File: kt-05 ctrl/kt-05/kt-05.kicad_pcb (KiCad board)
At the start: 4 copper layers, 50.3 x 71.2 mm, 76 parts, among them CN10 YTC1P-6030-01, CN11 YTC1P-6030-01, CN12 YTC1P-6030-01, CN13 YTC1P-6030-01, CN14 YTC1P-6030-01, CN15 MIDI IN, CN16 MIDI OUT, CN3 YTC1P-6030-01, CN4 Pogo Pin Receptor Right, CN5 YTC1P-6030-01, CN6 YTC1P-6030-01, CN7 YTC1P-6030-01, CN8 YTC1P-6030-01, CN9 YTC1P-6030-01, J1 Conn_01x06, Q1 AO3401A, Q2 AO3401A, Q3 AO3401A, SW1 ESP RST, SW2 ESP BOOT, U1 SK6812MINI-HS, U10 H3V3U10B, U11 H3V3U10B, U12 H3V3U10B, U13 H3V3U10B, U14 H3V3U10B, U15 H3V3U10B, U16 H3V3U10B, U17 H3V3U10B, U18 H3V3U10B, U19 H3V3U10B, U2 AP2112K-3.3, U20 H3V3U10B, U21 H3V3U10B, U22 H3V3U10B, U23 H3V3U10B, U3 MCP73831-2-OT, U4 PS-5850SVB-6PL, U5 H11L1S(TA), U6 ATtiny1616-M, U7 H3V3U10B, U8 ESP32-S3-MINI-1, U9 Pogo Pin Left

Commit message: ch
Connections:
- CN4 pad 1: SCL1 -> GND
- CN4 pad 2: SDA1 -> VRIGHT
- CN4 pad 3: VRIGHT -> SDA1
- CN4 pad 4: GND -> SCL1
- U9 pad 1: GND -> SCL0
- U9 pad 2: VLEFT -> SDA0
- U9 pad 3: SDA0 -> VLEFT
- U9 pad 4: SCL0 -> GND
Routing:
- net SCL0: track 55.4 -> 66.5 mm
- net SCL1: track 30.7 -> 38.8 mm
- net SDA0: track 62.2 -> 65.0 mm
- net GND: track 141.9 -> 140.0 mm, vias 96 -> 95
- net VLEFT: track 3.34 -> 4.82 mm, vias 0 -> 2
- net VRIGHT: track 3.27 -> 4.75 mm
- net SDA1: track 32.6 -> 33.2 mm, vias 3 -> 4

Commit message: many
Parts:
- added R10: 10K, Resistor_SMD:R_0402_1005Metric, F.Cu at (66.8, 36.6)
- added R11: 10K, Resistor_SMD:R_0402_1005Metric, F.Cu at (66.8, 38.6)
- moved J1 2.54 mm to (90.0, 84.6)
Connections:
- U8 pad 17: unconnected-(U8-IO13-Pad17) -> BAT_DET
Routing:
- net BAT_DET: track 0.00 -> 19.0 mm, vias 0 -> 2
- net VBAT: track 23.2 -> 27.7 mm
- net GND: track 140.0 -> 143.4 mm
- net SDA0: track 65.0 -> 67.5 mm
- net +3.3V: track 54.2 -> 56.7 mm
- net UPDI: track 74.5 -> 77.0 mm
- net SCL0: track 66.5 -> 69.0 mm
- net TXD: track 38.6 -> 40.5 mm
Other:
- outline, holes or cut-outs redrawn
- board text added: "0.1"
- board text added: "2/2026"
- board text added: "3.3V"
- board text added: "BATTERY HERE"
- board text added: "CC-BY-NC-SA 4.0"
- board text added: "CORE"
- board text added: "DESIGN"
- board text added: "ESP BOOT"
- board text added: "ESP RST"
- board text added: "GITHUB.COM/TORBERS"
- board text added: "GND"
- board text added: "IN"
- board text added: "MIDI"
- board text added: "OPEN SOURCE"
- board text added: "OUT"
- board text added: "POWER"
- board text added: "SCL"
- board text added: "SDA"
- board text added: "SHEPHERD MIX MODULE"
- board text added: "SOURCE FILES"
- board text added: "TEST TYPE"
- board text added: "TORBERS"
- board text added: "TXD"
- board text added: "TYPE-C"
- board text added: "UPDI"
- board text added: "USB"
- board text added: "VBUS"

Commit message: prod
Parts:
- moved R7 15.8 mm to (92.1, 57.3), turned to -90 degrees
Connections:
- U6 pad 1: A15 -> SCL0
- U6 pad 10: unconnected-(U6-PB4-Pad10) -> A16
- U6 pad 13: SDA0 -> A15
- U6 pad 14: SCL0 -> A14
- U6 pad 2: A16 -> unconnected-(U6-PA3-Pad2)
- U6 pad 20: A14 -> SDA0
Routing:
- net A15: track 6.33 -> 38.1 mm, vias 0 -> 4
- net A16: track 11.0 -> 21.8 mm, vias 0 -> 2
- net SCL0: track 69.0 -> 78.2 mm, vias 3 -> 5
- net A14: track 28.4 -> 37.5 mm, vias 2 -> 4
- net SDA0: track 67.5 -> 75.2 mm, vias 5 -> 7
- net UPDI: track 77.0 -> 78.0 mm
- net D10: track 8.93 -> 8.43 mm
- net GND: track 143.4 -> 143.5 mm, vias 95 -> 94

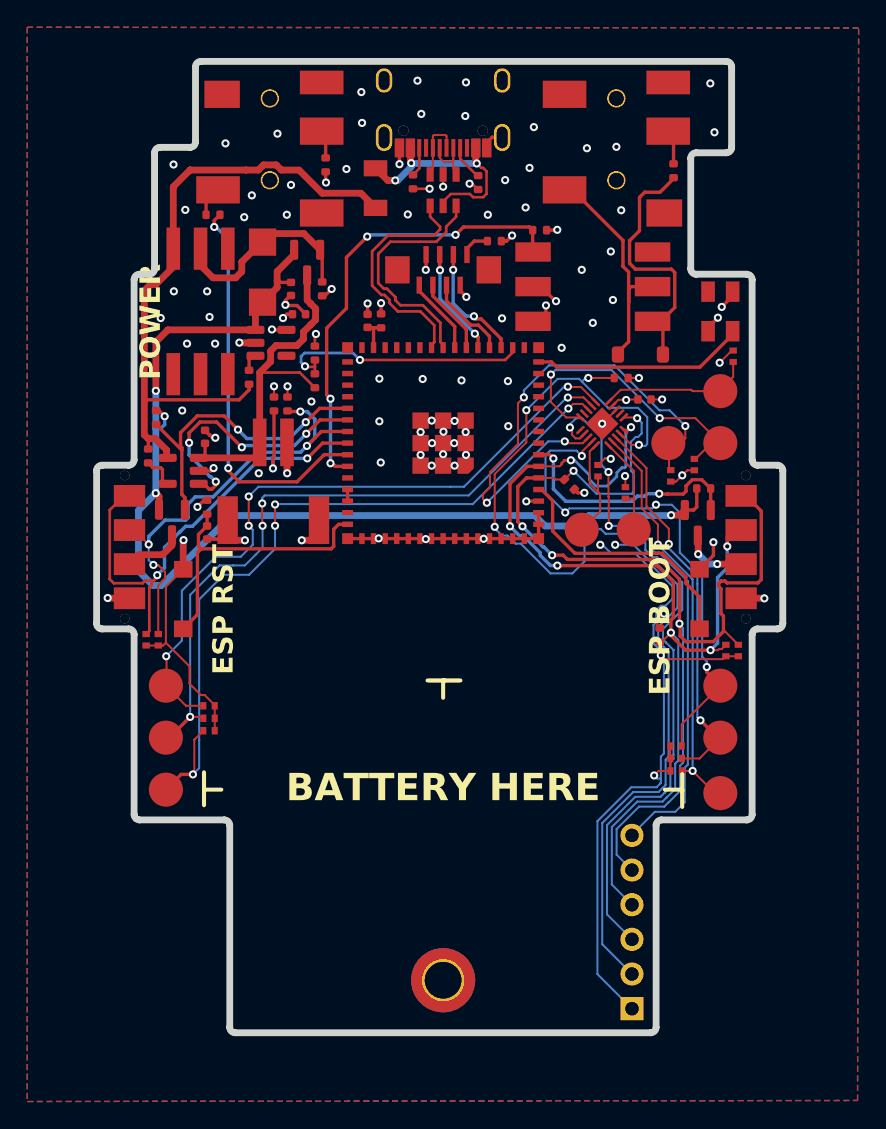
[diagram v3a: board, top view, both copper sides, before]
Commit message: improved fuses
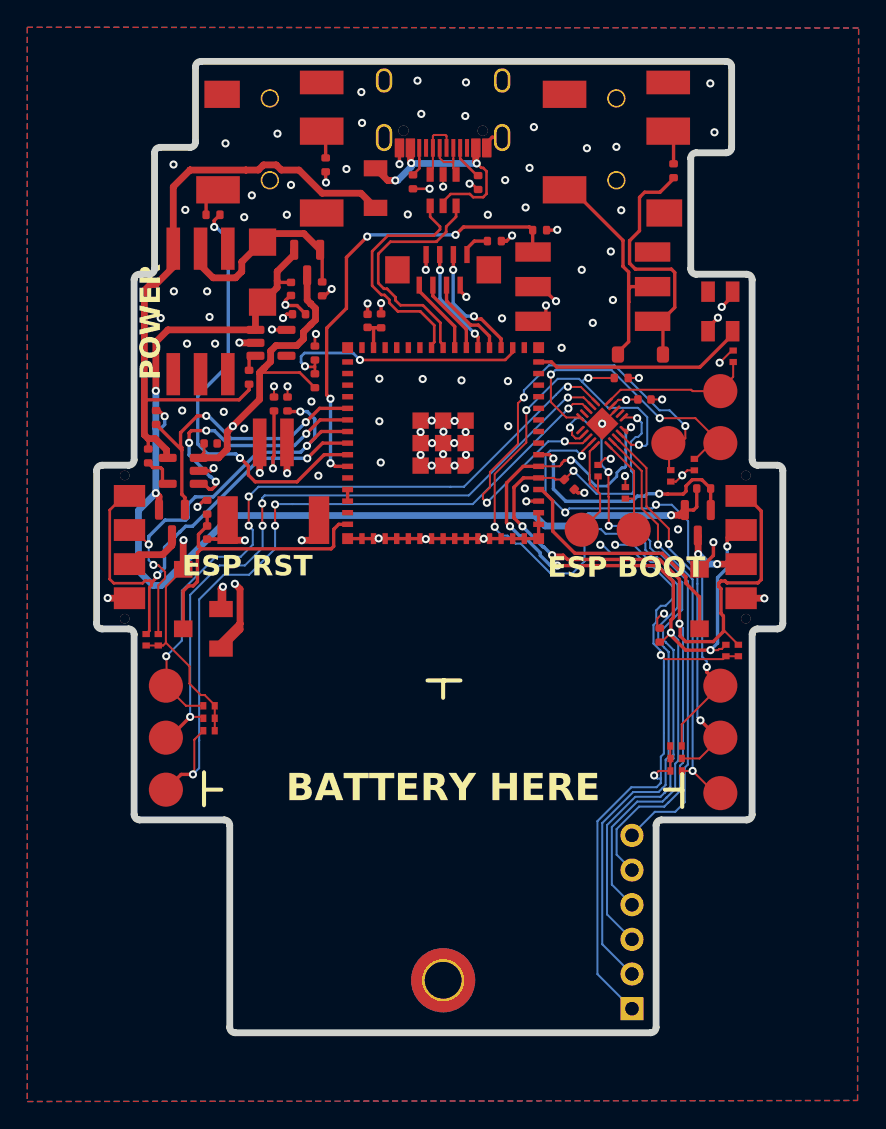
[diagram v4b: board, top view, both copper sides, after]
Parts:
- added F2: BSMD1206-200-6V, easyeda2kicad:F1206, F.Cu at (59.9, 56.8)
- moved C4 0.63 mm to (59.2, 43.2), turned to 0 degrees
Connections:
- H2 pad 1: VBAT -> Net-(F2-Pad2)
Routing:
- net Net-(F2-Pad2): track 0.00 -> 20.1 mm, vias 0 -> 2
- net VBAT: track 27.7 -> 40.8 mm, vias 0 -> 2
- net ESP_TXD0: track 29.4 -> 31.8 mm
- net GND: track 143.5 -> 142.5 mm, vias 94 -> 97
- net CG_STAT: track 19.8 -> 19.1 mm

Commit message: production 1
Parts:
- added C7: 1u, Capacitor_SMD:C_0402_1005Metric, F.Cu at (85.1, 36.5)
- added C8: 10u, Capacitor_SMD:C_0402_1005Metric, F.Cu at (86.1, 36.5)
- added C9: 10u, Capacitor_SMD:C_0402_1005Metric, F.Cu at (87.1, 36.5)
- added G***: LOGO, LOGO, F.Cu at (76.2, 76.2)
- added G***: LOGO, LOGO, B.Cu at (58.5, 60.7)
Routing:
- net GND: track 142.5 -> 146.9 mm, vias 97 -> 104
- net +3.3V: track 57.1 -> 60.1 mm, vias 17 -> 20
- net UPDI: track 78.0 -> 78.9 mm
- net A15: track 38.1 -> 38.9 mm
- net A16: track 21.8 -> 22.6 mm
- net VHIGH: track 82.3 -> 82.9 mm
- net NEO: track 15.6 -> 15.3 mm, vias 0 -> 2
- net A14: track 37.5 -> 37.3 mm, vias 4 -> 3
